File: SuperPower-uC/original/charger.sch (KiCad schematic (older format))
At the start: 31 parts, among them J1 Conn_01x02_Male, Q1 Q_NMOS_DGS, Q2 Q_NMOS_DGS, Q3 Q_NMOS_DGS, Q4 Q_PMOS_DGS, U1 LTC4162-L

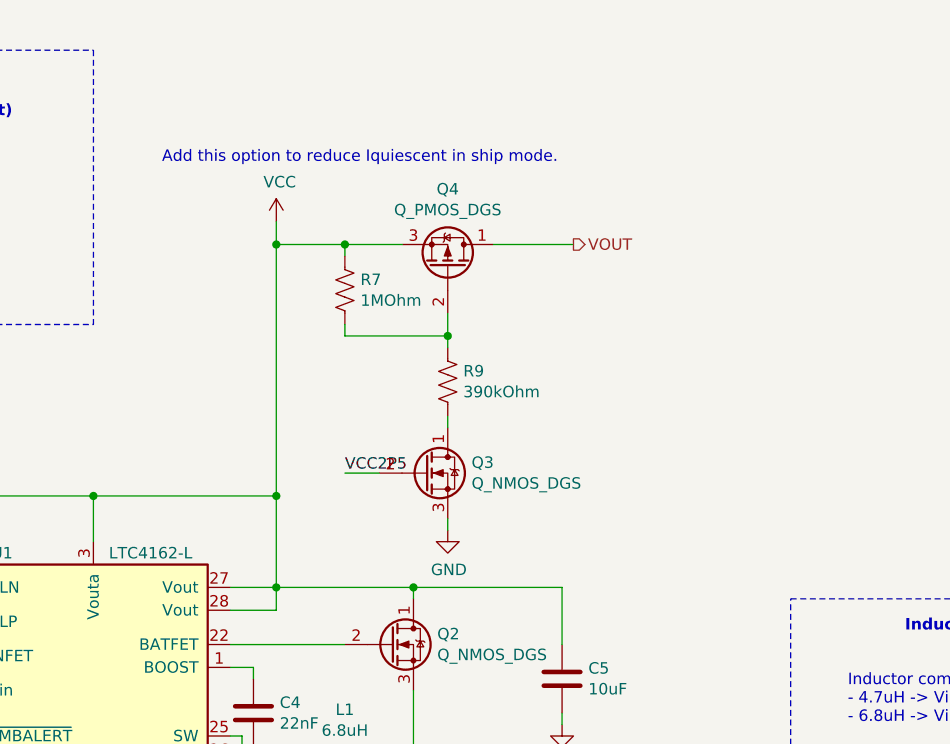
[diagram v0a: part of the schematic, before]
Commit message: Add the possibility to bypass the extra low quiescent current option
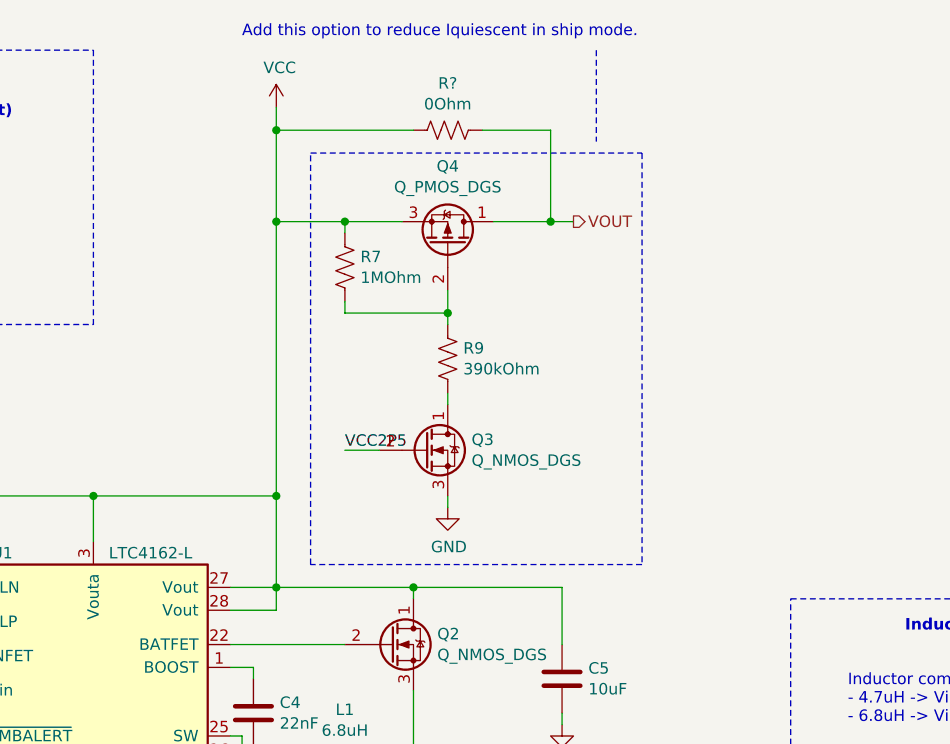
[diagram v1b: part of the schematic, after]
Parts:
- added R?: 0Ohm, symbol Device:R_US
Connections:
- net VCC: now also R?.2
- net VOUT: now also R?.1
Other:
- moved on the sheet: Q3, Q4, R7, R9
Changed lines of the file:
@@
 Text HLabel 1350 2900 0    50   Input ~ 0
 VSOLAR_IN
-Text HLabel 7700 1600 2    50   Output ~ 0
+Text HLabel 7700 1500 2    50   Output ~ 0
 VOUT
 Text HLabel 8000 4350 2    50   BiDi ~ 0
@@
 L power:VCC #PWR09
 U 1 1 5F745F21
-P 6400 1500
-F 0 "#PWR09" H 6400 1350 50  0001 C CNN
-F 1 "VCC" H 6415 1673 50  0000 C CNN
-F 2 "" H 6400 1500 50  0001 C CNN
-F 3 "" H 6400 1500 50  0001 C CNN
-	1    6400 1500
+P 6400 1000
+F 0 "#PWR09" H 6400 850 50  0001 C CNN
+F 1 "VCC" H 6415 1173 50  0000 C CNN
+F 2 "" H 6400 1000 50  0001 C CNN
+F 3 "" H 6400 1000 50  0001 C CNN
+	1    6400 1000
 	1    0    0    -1
 $EndComp
@@
 Wire Wire Line
 	5600 2700 6400 2700
-Wire Wire Line
-	6400 2700 6400 3100
 Connection ~ 5600 2700
 Connection ~ 6400 3100
@@
 Wire Wire Line
 	7000 3100 7000 3150
-Wire Wire Line
-	6400 1500 6400 1600
 Connection ~ 6400 2700
 $Comp
@@
 	7650 3100 7000 3100
 Connection ~ 7000 3100
-Text Notes 5900 1250 0    50   ~ 0
+Text Notes 6250 700  0    50   ~ 0
 Add this option to reduce Iquiescent in ship mode.
 Wire Wire Line
@@
 L Device:Q_PMOS_DGS Q4
 U 1 1 5F8471F5
-P 7150 1700
-F 0 "Q4" V 7492 1700 50  0000 C CNN
-F 1 "Q_PMOS_DGS" V 7401 1700 50  0000 C CNN
-F 2 "" H 7350 1800 50  0001 C CNN
-F 3 "~" H 7150 1700 50  0001 C CNN
-	1    7150 1700
+P 7150 1600
+F 0 "Q4" V 7492 1600 50  0000 C CNN
+F 1 "Q_PMOS_DGS" V 7401 1600 50  0000 C CNN
+F 2 "" H 7350 1700 50  0001 C CNN
+F 3 "~" H 7150 1600 50  0001 C CNN
+	1    7150 1600
 	0    1    -1   0
 $EndComp
@@
 L Device:Q_NMOS_DGS Q3
 U 1 1 5F84F43E
-P 7050 2600
-F 0 "Q3" H 7254 2646 50  0000 L CNN
-F 1 "Q_NMOS_DGS" H 7254 2555 50  0000 L CNN
-F 2 "" H 7250 2700 50  0001 C CNN
-F 3 "~" H 7050 2600 50  0001 C CNN
-	1    7050 2600
+P 7050 2500
+F 0 "Q3" H 7254 2546 50  0000 L CNN
+F 1 "Q_NMOS_DGS" H 7254 2455 50  0000 L CNN
+F 2 "" H 7250 2600 50  0001 C CNN
+F 3 "~" H 7050 2500 50  0001 C CNN
+	1    7050 2500
 	1    0    0    -1
 $EndComp
@@
 L Device:R_US R9
 U 1 1 5F8508E1
-P 7150 2200
-F 0 "R9" H 7218 2246 50  0000 L CNN
-F 1 "390kOhm" H 7218 2155 50  0000 L CNN
-F 2 "" V 7190 2190 50  0001 C CNN
-F 3 "~" H 7150 2200 50  0001 C CNN
-	1    7150 2200
+P 7150 2100
+F 0 "R9" H 7218 2146 50  0000 L CNN
+F 1 "390kOhm" H 7218 2055 50  0000 L CNN
+F 2 "" V 7190 2090 50  0001 C CNN
+F 3 "~" H 7150 2100 50  0001 C CNN
+	1    7150 2100
 	1    0    0    -1
 $EndComp
 Wire Wire Line
-	7150 1900 7150 2000
+	7150 1800 7150 1900
 Wire Wire Line
-	7150 2400 7150 2350
+	7150 2300 7150 2250
 $Comp
 L Device:R_US R7
 U 1 1 5F85C6FA
-P 6700 1800
-F 0 "R7" H 6768 1846 50  0000 L CNN
-F 1 "1MOhm" H 6768 1755 50  0000 L CNN
-F 2 "" V 6740 1790 50  0001 C CNN
-F 3 "~" H 6700 1800 50  0001 C CNN
-	1    6700 1800
+P 6700 1700
+F 0 "R7" H 6768 1746 50  0000 L CNN
+F 1 "1MOhm" H 6768 1655 50  0000 L CNN
+F 2 "" V 6740 1690 50  0001 C CNN
+F 3 "~" H 6700 1700 50  0001 C CNN
+	1    6700 1700
 	1    0    0    -1
 $EndComp
 Wire Wire Line
-	6950 1600 6700 1600
+	6950 1500 6700 1500
 Wire Wire Line
-	6700 1600 6700 1650
+	6700 1500 6700 1550
 Wire Wire Line
-	6700 2000 7150 2000
-Connection ~ 7150 2000
+	6700 1900 7150 1900
+Connection ~ 7150 1900
 Wire Wire Line
-	7150 2000 7150 2050
+	7150 1900 7150 1950
 Wire Wire Line
-	6700 1950 6700 2000
+	6700 1850 6700 1900
 $Comp
 L power:GND #PWR012
 U 1 1 5F880629
-P 7150 2850
-F 0 "#PWR012" H 7150 2600 50  0001 C CNN
-F 1 "GND" H 7155 2677 50  0000 C CNN
-F 2 "" H 7150 2850 50  0001 C CNN
-F 3 "" H 7150 2850 50  0001 C CNN
-	1    7150 2850
+P 7150 2750
+F 0 "#PWR012" H 7150 2500 50  0001 C CNN
+F 1 "GND" H 7155 2577 50  0000 C CNN
+F 2 "" H 7150 2750 50  0001 C CNN
+F 3 "" H 7150 2750 50  0001 C CNN
+	1    7150 2750
 	1    0    0    -1
 $EndComp
 Wire Wire Line
-	7150 2800 7150 2850
+	7150 2700 7150 2750
 Wire Wire Line
-	7350 1600 7700 1600
-Text Label 6700 2600 0    50   ~ 0
+	7350 1500 7600 1500
+Text Label 6700 2500 0    50   ~ 0
 VCC2P5
 Wire Wire Line
-	6700 2600 6850 2600
+	6700 2500 6850 2500
 Wire Wire Line
-	6700 1600 6400 1600
-Connection ~ 6700 1600
-Connection ~ 6400 1600
-Wire Wire Line
-	6400 1600 6400 2700
+	6700 1500 6400 1500
+Connection ~ 6700 1500
 $Comp
 L Device:LED_ARGB D1
@@
 Text Notes 9450 5550 0    50   ~ 0
 External Battery connector
+$Comp
+L Device:R_US R?
+U 1 1 5F8322FE
+P 7150 1100
+F 0 "R?" V 6945 1100 50  0000 C CNN
+F 1 "0Ohm" V 7036 1100 50  0000 C CNN
+F 2 "" V 7190 1090 50  0001 C CNN
+F 3 "~" H 7150 1100 50  0001 C CNN
+	1    7150 1100
+	0    1    1    0
+$EndComp
+Wire Wire Line
+	7300 1100 7600 1100
+Wire Wire Line
+	7600 1100 7600 1500
+Connection ~ 7600 1500
+Wire Wire Line
+	7600 1500 7700 1500
+Wire Notes Line
+	6550 1200 8000 1200
+Wire Notes Line
+	8000 1200 8000 3000
+Wire Notes Line
+	8000 3000 6550 3000
+Wire Notes Line
+	6550 3000 6550 1200
+Wire Wire Line
+	6400 2700 6400 3100
+Connection ~ 6400 1500
+Wire Wire Line
+	6400 1000 6400 1100
+Wire Wire Line
+	6400 1500 6400 2700
+Wire Wire Line
+	7000 1100 6400 1100
+Connection ~ 6400 1100
+Wire Wire Line
+	6400 1100 6400 1500
+Wire Notes Line
+	7800 750  7800 1150
 $EndSCHEMATC

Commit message: Annotate components to solve problems.
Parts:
- gave numbers to parts that had none: 2
- renumbered R9 to R10
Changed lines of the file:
@@
 $EndComp
 $Comp
-L Device:R_US R9
+L Device:R_US R10
 U 1 1 5F8508E1
 P 7150 2100
-F 0 "R9" H 7218 2146 50  0000 L CNN
+F 0 "R10" H 7218 2146 50  0000 L CNN
 F 1 "390kOhm" H 7218 2055 50  0000 L CNN
 F 2 "" V 7190 2090 50  0001 C CNN
@@
 TODO :\nAdd Hierachical Block Connectors
 $Comp
-L Connector:Conn_01x02_Male J?
+L Connector:Conn_01x02_Male J2
 U 1 1 5F831EE9
 P 9650 5950
-F 0 "J?" H 9622 5924 50  0000 R CNN
+F 0 "J2" H 9622 5924 50  0000 R CNN
 F 1 "Conn_01x02_Male" H 9622 5833 50  0000 R CNN
 F 2 "" H 9650 5950 50  0001 C CNN
@@
 $EndComp
 $Comp
-L power:GND #PWR?
+L power:GND #PWR016
 U 1 1 5F831EF3
 P 9350 6150
-F 0 "#PWR?" H 9350 5900 50  0001 C CNN
+F 0 "#PWR016" H 9350 5900 50  0001 C CNN
 F 1 "GND" H 9355 5977 50  0000 C CNN
 F 2 "" H 9350 6150 50  0001 C CNN
@@
 	9350 5950 9350 5850
 $Comp
-L power:+BATT #PWR?
+L power:+BATT #PWR015
 U 1 1 5F837E39
 P 9350 5850
-F 0 "#PWR?" H 9350 5700 50  0001 C CNN
+F 0 "#PWR015" H 9350 5700 50  0001 C CNN
 F 1 "+BATT" H 9365 6023 50  0000 C CNN
 F 2 "" H 9350 5850 50  0001 C CNN
@@
 External Battery connector
 $Comp
-L Device:R_US R?
+L Device:R_US R9
 U 1 1 5F8322FE
 P 7150 1100
-F 0 "R?" V 6945 1100 50  0000 C CNN
+F 0 "R9" V 6945 1100 50  0000 C CNN
 F 1 "0Ohm" V 7036 1100 50  0000 C CNN
 F 2 "" V 7190 1090 50  0001 C CNN

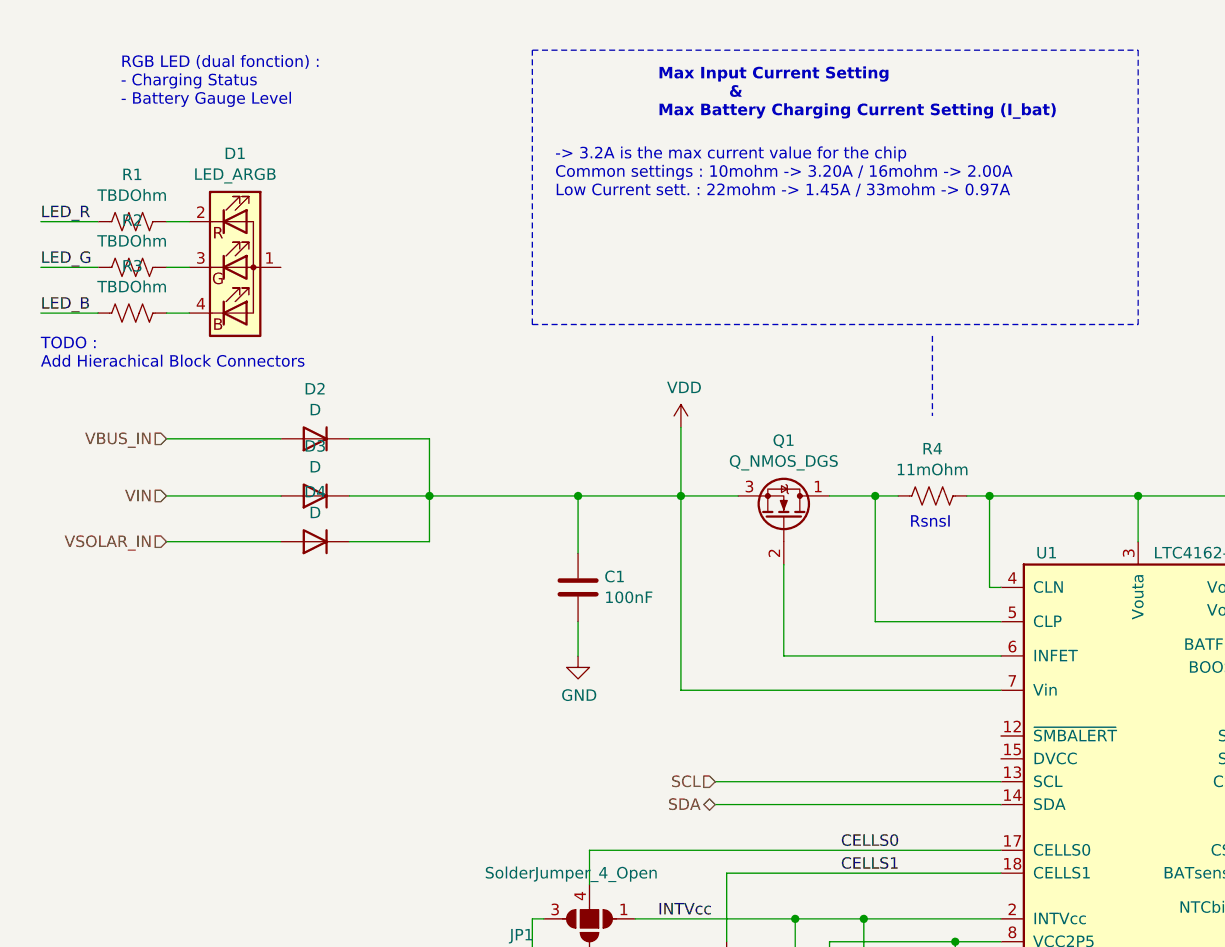
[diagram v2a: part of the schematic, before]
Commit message: Adding an optional LED on the LTC4162-L SMBALERT output
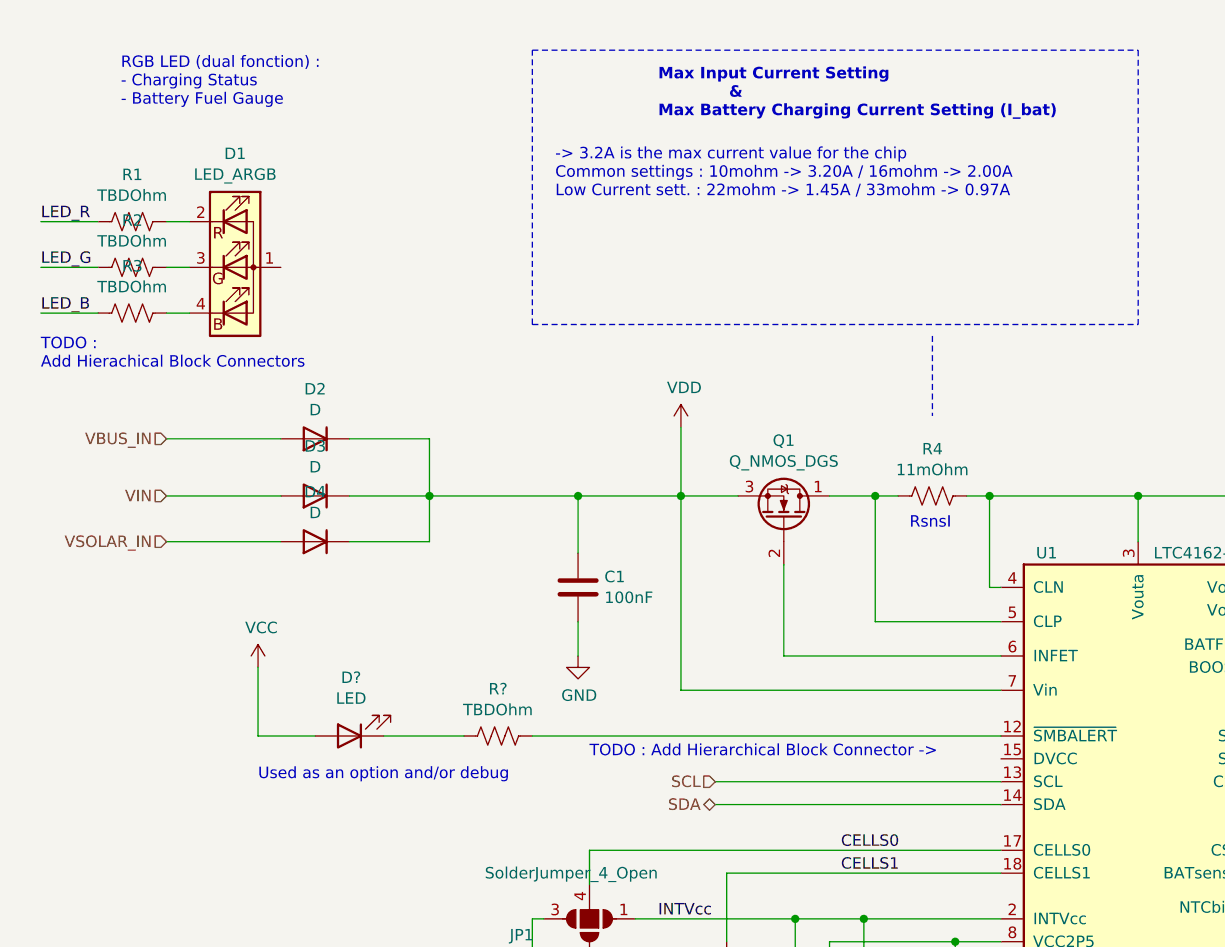
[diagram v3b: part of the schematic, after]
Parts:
- added D?: LED, symbol Device:LED
- added R?: TBDOhm, symbol Device:R_US
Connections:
- net VCC: now also D?.2 (A)
- net at U1.12 (~SMBALERT): now also R?.1
- new net: D?.1 (K), R?.2
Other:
- note added: "RGB LED (dual fonction) :\n- Charging Status\n- Battery Fuel Gauge"
- note added: "TODO : Add Hierarchical Block Connector ->"
- note added: "Used as an option and/or debug"
- note removed: "RGB LED (dual fonction) :\n- Charging Status\n- Battery Gauge Level"
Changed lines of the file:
@@
 	1350 1900 1450 1900
 Text Notes 1150 1000 0    50   ~ 0
-RGB LED (dual fonction) :\n- Charging Status\n- Battery Gauge Level
+RGB LED (dual fonction) :\n- Charging Status\n- Battery Fuel Gauge
 Text Label 800  1500 0    50   ~ 0
 LED_R
@@
 Wire Notes Line
 	7800 750  7800 1150
+$Comp
+L Device:LED D?
+U 1 1 5F83318B
+P 2150 3750
+F 0 "D?" H 2143 3495 50  0000 C CNN
+F 1 "LED" H 2143 3586 50  0000 C CNN
+F 2 "" H 2150 3750 50  0001 C CNN
+F 3 "~" H 2150 3750 50  0001 C CNN
+	1    2150 3750
+	-1   0    0    1
+$EndComp
+$Comp
+L Device:R_US R?
+U 1 1 5F84595F
+P 2800 3750
+F 0 "R?" V 2595 3750 50  0000 C CNN
+F 1 "TBDOhm" V 2686 3750 50  0000 C CNN
+F 2 "" V 2840 3740 50  0001 C CNN
+F 3 "~" H 2800 3750 50  0001 C CNN
+	1    2800 3750
+	0    1    1    0
+$EndComp
+Wire Wire Line
+	5000 3750 2950 3750
+Wire Wire Line
+	2300 3750 2650 3750
+$Comp
+L power:VCC #PWR?
+U 1 1 5F851525
+P 1750 3450
+F 0 "#PWR?" H 1750 3300 50  0001 C CNN
+F 1 "VCC" H 1765 3623 50  0000 C CNN
+F 2 "" H 1750 3450 50  0001 C CNN
+F 3 "" H 1750 3450 50  0001 C CNN
+	1    1750 3450
+	1    0    0    -1
+$EndComp
+Wire Wire Line
+	2000 3750 1750 3750
+Wire Wire Line
+	1750 3750 1750 3450
+Text Notes 1750 3950 0    50   ~ 0
+Used as an option and/or debug
+Text Notes 3200 3850 0    50   ~ 0
+TODO : Add Hierarchical Block Connector ->
 $EndSCHEMATC

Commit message: Annotate new components
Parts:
- gave numbers to parts that had none: 2
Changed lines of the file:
@@
 	7800 750  7800 1150
 $Comp
-L Device:LED D?
+L Device:LED D5
 U 1 1 5F83318B
 P 2150 3750
-F 0 "D?" H 2143 3495 50  0000 C CNN
+F 0 "D5" H 2143 3495 50  0000 C CNN
 F 1 "LED" H 2143 3586 50  0000 C CNN
 F 2 "" H 2150 3750 50  0001 C CNN
@@
 $EndComp
 $Comp
-L Device:R_US R?
+L Device:R_US R18
 U 1 1 5F84595F
 P 2800 3750
-F 0 "R?" V 2595 3750 50  0000 C CNN
+F 0 "R18" V 2595 3750 50  0000 C CNN
 F 1 "TBDOhm" V 2686 3750 50  0000 C CNN
 F 2 "" V 2840 3740 50  0001 C CNN
@@
 	2300 3750 2650 3750
 $Comp
-L power:VCC #PWR?
+L power:VCC #PWR027
 U 1 1 5F851525
 P 1750 3450
-F 0 "#PWR?" H 1750 3300 50  0001 C CNN
+F 0 "#PWR027" H 1750 3300 50  0001 C CNN
 F 1 "VCC" H 1765 3623 50  0000 C CNN
 F 2 "" H 1750 3450 50  0001 C CNN
